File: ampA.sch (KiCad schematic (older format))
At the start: 13 parts, among them U2 screw_term, U3 screw_term, U4 screw_term, U7 TL084

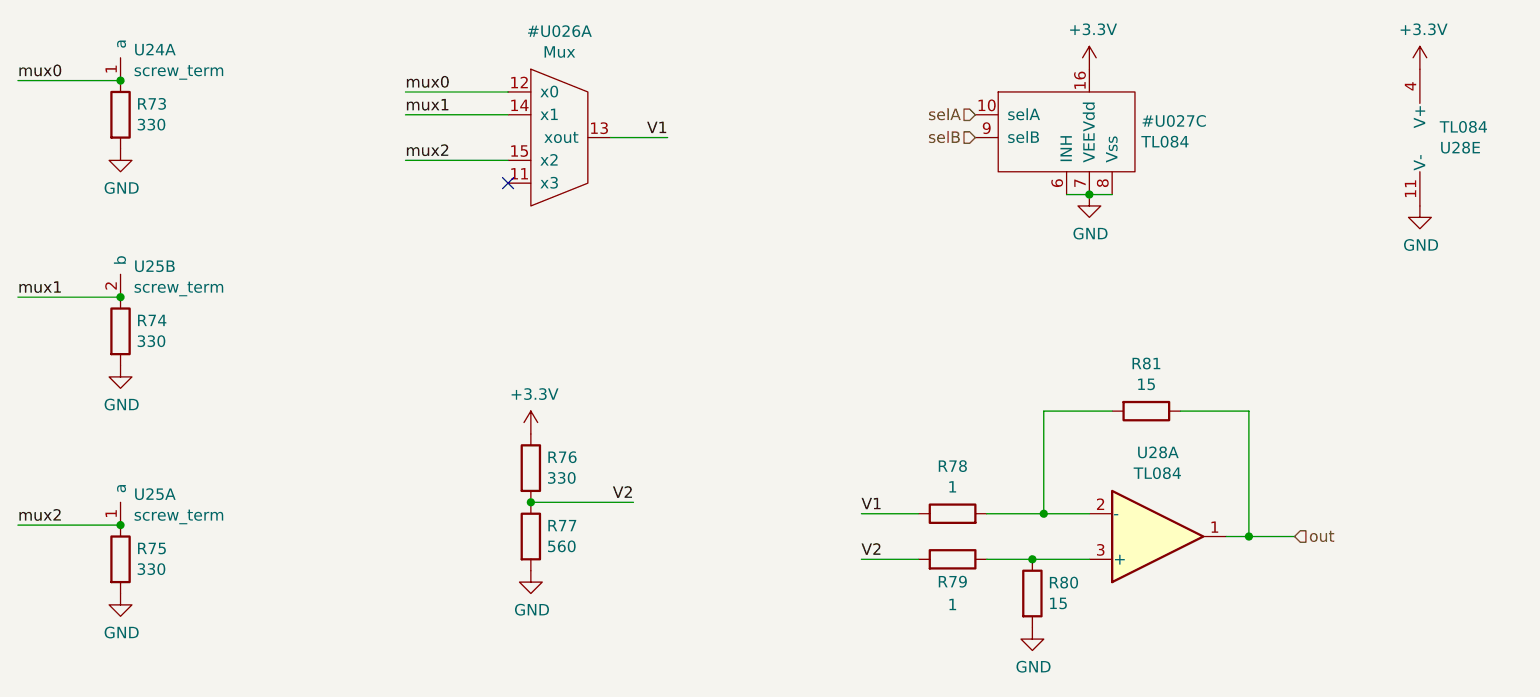
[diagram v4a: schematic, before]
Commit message: added footprint to some op amps
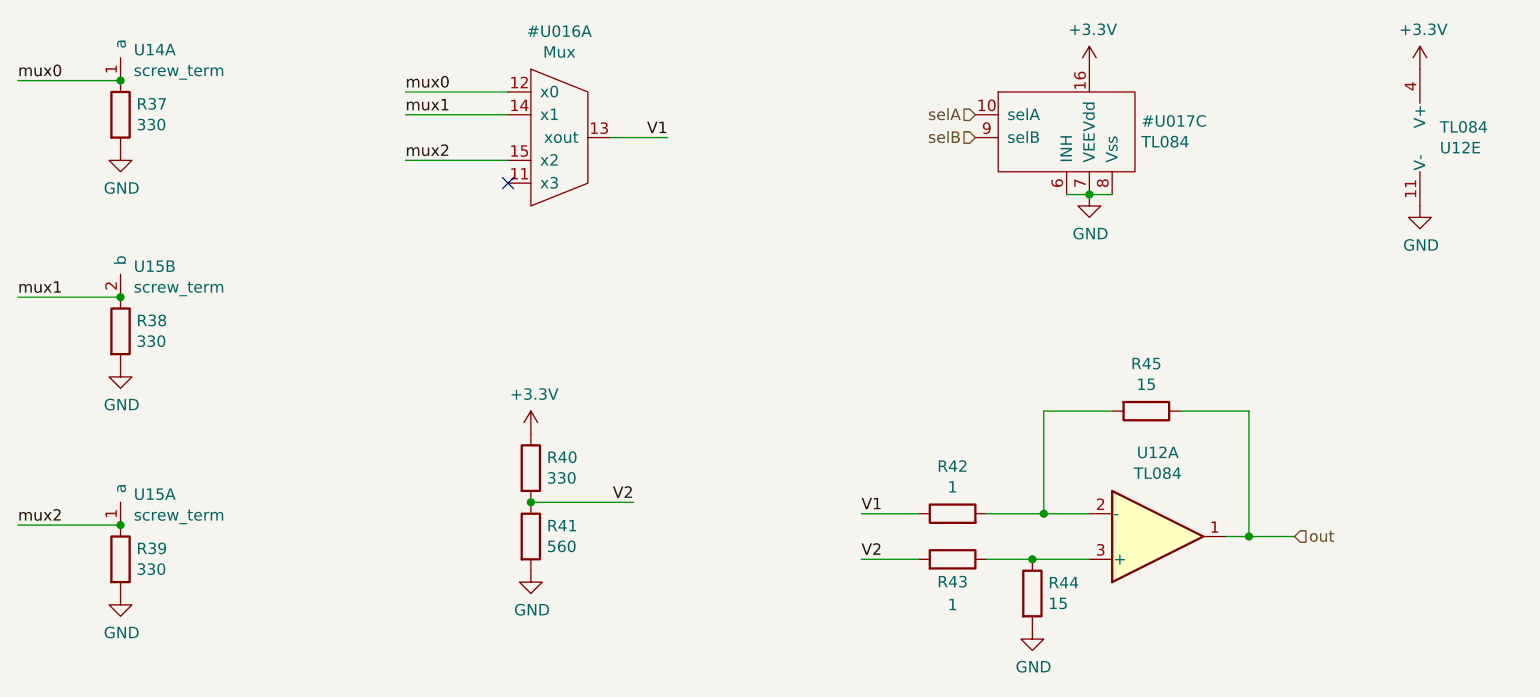
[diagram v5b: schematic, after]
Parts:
- U7: footprint (none) -> Package_DIP:DIP-14_W7.62mm
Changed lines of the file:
@@
 AR Path="/601B4C0E/6013BAC9" Ref="#PWR038"  Part="1"
 AR Path="/601B73B7/6013BAC9" Ref="#PWR068"  Part="1"
-F 0 "#PWR068" H 1450 1850 50  0001 C CNN
+F 0 "#PWR038" H 1450 1850 50  0001 C CNN
 F 1 "GND" H 1455 1927 50  0000 C CNN
 F 2 "" H 1450 2100 50  0001 C CNN
@@
 AR Path="/601B4C0E/60198F31" Ref="U12"  Part="1"
 AR Path="/601B73B7/60198F31" Ref="U28"  Part="1"
-F 0 "U28" H 6000 3433 50  0000 C CNN
+F 0 "U12" H 6000 3433 50  0000 C CNN
 F 1 "TL084" H 6000 3524 50  0000 C CNN
-F 2 "" H 5950 3900 50  0001 C CNN
+F 2 "Package_DIP:DIP-14_W7.62mm" H 5950 3900 50  0001 C CNN
 F 3 "http://www.ti.com/lit/ds/symlink/tl081.pdf" H 6050 4000 50  0001 C CNN
 	1    6000 3800
@@
 AR Path="/601B4C0E/6019D565" Ref="R44"  Part="1"
 AR Path="/601B73B7/6019D565" Ref="R80"  Part="1"
-F 0 "R80" H 5520 4096 50  0000 L CNN
+F 0 "R44" H 5520 4096 50  0000 L CNN
 F 1 "15" H 5520 4005 50  0000 L CNN
 F 2 "Resistor_THT:R_Axial_DIN0204_L3.6mm_D1.6mm_P5.08mm_Horizontal" V 5380 4050 50  0001 C CNN
@@
 AR Path="/601B4C0E/60198F32" Ref="R45"  Part="1"
 AR Path="/601B73B7/60198F32" Ref="R81"  Part="1"
-F 0 "R81" V 5743 3250 50  0000 C CNN
+F 0 "R45" V 5743 3250 50  0000 C CNN
 F 1 "15" V 5834 3250 50  0000 C CNN
 F 2 "Resistor_THT:R_Axial_DIN0204_L3.6mm_D1.6mm_P5.08mm_Horizontal" V 5880 3250 50  0001 C CNN
@@
 AR Path="/601B4C0E/6017E431" Ref="R42"  Part="1"
 AR Path="/601B73B7/6017E431" Ref="R78"  Part="1"
-F 0 "R78" V 5307 3700 50  0000 C CNN
+F 0 "R42" V 5307 3700 50  0000 C CNN
 F 1 "1" V 5216 3700 50  0000 C CNN
 F 2 "Resistor_THT:R_Axial_DIN0204_L3.6mm_D1.6mm_P5.08mm_Horizontal" V 5030 3700 50  0001 C CNN
@@
 AR Path="/601B4C0E/6019D568" Ref="R43"  Part="1"
 AR Path="/601B73B7/6019D568" Ref="R79"  Part="1"
-F 0 "R79" V 5000 3900 50  0000 C CNN
+F 0 "R43" V 5000 3900 50  0000 C CNN
 F 1 "1" V 4900 3900 50  0000 C CNN
 F 2 "Resistor_THT:R_Axial_DIN0204_L3.6mm_D1.6mm_P5.08mm_Horizontal" V 5030 3900 50  0001 C CNN
@@
 AR Path="/601B4C0E/6019D55E" Ref="R40"  Part="1"
 AR Path="/601B73B7/6019D55E" Ref="R76"  Part="1"
-F 0 "R76" H 3320 3546 50  0000 L CNN
+F 0 "R40" H 3320 3546 50  0000 L CNN
 F 1 "330" H 3320 3455 50  0000 L CNN
 F 2 "Resistor_THT:R_Axial_DIN0204_L3.6mm_D1.6mm_P5.08mm_Horizontal" V 3180 3500 50  0001 C CNN
@@
 AR Path="/601B4C0E/6019D55F" Ref="R41"  Part="1"
 AR Path="/601B73B7/6019D55F" Ref="R77"  Part="1"
-F 0 "R77" H 3320 3846 50  0000 L CNN
+F 0 "R41" H 3320 3846 50  0000 L CNN
 F 1 "560" H 3320 3755 50  0000 L CNN
 F 2 "Resistor_THT:R_Axial_DIN0204_L3.6mm_D1.6mm_P5.08mm_Horizontal" V 3180 3800 50  0001 C CNN
@@
 AR Path="/601B4C0E/6019D560" Ref="#PWR041"  Part="1"
 AR Path="/601B73B7/6019D560" Ref="#PWR071"  Part="1"
-F 0 "#PWR071" H 3250 3200 50  0001 C CNN
+F 0 "#PWR041" H 3250 3200 50  0001 C CNN
 F 1 "+3.3V" H 3265 3523 50  0000 C CNN
 F 2 "" H 3250 3350 50  0001 C CNN
@@
 AR Path="/601B4C0E/60198F38" Ref="#PWR042"  Part="1"
 AR Path="/601B73B7/60198F38" Ref="#PWR072"  Part="1"
-F 0 "#PWR072" H 3250 3700 50  0001 C CNN
+F 0 "#PWR042" H 3250 3700 50  0001 C CNN
 F 1 "GND" H 3255 3777 50  0000 C CNN
 F 2 "" H 3250 3950 50  0001 C CNN
@@
 AR Path="/601B4C0E/6016B854" Ref="#PWR043"  Part="1"
 AR Path="/601B73B7/6016B854" Ref="#PWR073"  Part="1"
-F 0 "#PWR073" H 5450 3950 50  0001 C CNN
+F 0 "#PWR043" H 5450 3950 50  0001 C CNN
 F 1 "GND" H 5455 4027 50  0000 C CNN
 F 2 "" H 5450 4200 50  0001 C CNN
@@
 AR Path="/601B4C0E/6016D691" Ref="R37"  Part="1"
 AR Path="/601B73B7/6016D691" Ref="R73"  Part="1"
-F 0 "R73" H 1520 1996 50  0000 L CNN
+F 0 "R37" H 1520 1996 50  0000 L CNN
 F 1 "330" H 1520 1905 50  0000 L CNN
 F 2 "Resistor_THT:R_Axial_DIN0204_L3.6mm_D1.6mm_P5.08mm_Horizontal" V 1380 1950 50  0001 C CNN
@@
 AR Path="/601B4C0E/601709E6" Ref="#U016"  Part="1"
 AR Path="/601B73B7/601709E6" Ref="#U026"  Part="1"
-F 0 "#U026" H 3375 2515 50  0000 C CNN
+F 0 "#U016" H 3375 2515 50  0000 C CNN
 F 1 "Mux" H 3375 2424 50  0000 C CNN
 F 2 "Package_DIP:DIP-14_W7.62mm" H 3350 2050 50  0001 C CNN
@@
 AR Path="/601B4C0E/6016FA62" Ref="U14"  Part="1"
 AR Path="/601B73B7/6016FA62" Ref="U24"  Part="1"
-F 0 "U24" H 1508 1934 50  0000 L CNN
+F 0 "U14" H 1508 1934 50  0000 L CNN
 F 1 "screw_term" H 1508 1843 50  0000 L CNN
 F 2 "Connector_PinHeader_1.27mm:PinHeader_1x02_P1.27mm_Vertical" H 1450 1800 50  0001 C CNN
@@
 AR Path="/601B4C0E/6019D559" Ref="#PWR039"  Part="1"
 AR Path="/601B73B7/6019D559" Ref="#PWR069"  Part="1"
-F 0 "#PWR069" H 1450 2800 50  0001 C CNN
+F 0 "#PWR039" H 1450 2800 50  0001 C CNN
 F 1 "GND" H 1455 2877 50  0000 C CNN
 F 2 "" H 1450 3050 50  0001 C CNN
@@
 AR Path="/601B4C0E/6019D56A" Ref="R38"  Part="1"
 AR Path="/601B73B7/6019D56A" Ref="R74"  Part="1"
-F 0 "R74" H 1520 2946 50  0000 L CNN
+F 0 "R38" H 1520 2946 50  0000 L CNN
 F 1 "330" H 1520 2855 50  0000 L CNN
 F 2 "Resistor_THT:R_Axial_DIN0204_L3.6mm_D1.6mm_P5.08mm_Horizontal" V 1380 2900 50  0001 C CNN
@@
 AR Path="/601B4C0E/60176F25" Ref="U15"  Part="2"
 AR Path="/601B73B7/60176F25" Ref="U25"  Part="2"
-F 0 "U25" H 1508 2884 50  0000 L CNN
+F 0 "U15" H 1508 2884 50  0000 L CNN
 F 1 "screw_term" H 1508 2793 50  0000 L CNN
 F 2 "Connector_PinHeader_1.27mm:PinHeader_1x02_P1.27mm_Vertical" H 1450 2750 50  0001 C CNN
@@
 AR Path="/601B4C0E/6019D55B" Ref="#PWR040"  Part="1"
 AR Path="/601B73B7/6019D55B" Ref="#PWR070"  Part="1"
-F 0 "#PWR070" H 1450 3800 50  0001 C CNN
+F 0 "#PWR040" H 1450 3800 50  0001 C CNN
 F 1 "GND" H 1455 3877 50  0000 C CNN
 F 2 "" H 1450 4050 50  0001 C CNN
@@
 AR Path="/601B4C0E/6017E43F" Ref="R39"  Part="1"
 AR Path="/601B73B7/6017E43F" Ref="R75"  Part="1"
-F 0 "R75" H 1520 3946 50  0000 L CNN
+F 0 "R39" H 1520 3946 50  0000 L CNN
 F 1 "330" H 1520 3855 50  0000 L CNN
 F 2 "Resistor_THT:R_Axial_DIN0204_L3.6mm_D1.6mm_P5.08mm_Horizontal" V 1380 3900 50  0001 C CNN
@@
 AR Path="/601B4C0E/6019D55C" Ref="U15"  Part="1"
 AR Path="/601B73B7/6019D55C" Ref="U25"  Part="1"
-F 0 "U25" H 1508 3884 50  0000 L CNN
+F 0 "U15" H 1508 3884 50  0000 L CNN
 F 1 "screw_term" H 1508 3793 50  0000 L CNN
 F 2 "Connector_PinHeader_1.27mm:PinHeader_1x02_P1.27mm_Vertical" H 1450 3750 50  0001 C CNN
@@
 AR Path="/601B4C0E/60186A46" Ref="#U017"  Part="3"
 AR Path="/601B73B7/60186A46" Ref="#U027"  Part="3"
-F 0 "#U027" H 5928 2221 50  0000 L CNN
+F 0 "#U017" H 5928 2221 50  0000 L CNN
 F 1 "TL084" H 5928 2130 50  0000 L CNN
 F 2 "" H 5700 2100 50  0001 C CNN
@@
 AR Path="/601B4C0E/601899DD" Ref="#PWR045"  Part="1"
 AR Path="/601B73B7/601899DD" Ref="#PWR075"  Part="1"
-F 0 "#PWR075" H 5700 2050 50  0001 C CNN
+F 0 "#PWR045" H 5700 2050 50  0001 C CNN
 F 1 "GND" H 5705 2127 50  0000 C CNN
 F 2 "" H 5700 2300 50  0001 C CNN
@@
 AR Path="/601B4C0E/60189E9E" Ref="#PWR044"  Part="1"
 AR Path="/601B73B7/60189E9E" Ref="#PWR074"  Part="1"
-F 0 "#PWR074" H 5700 1600 50  0001 C CNN
+F 0 "#PWR044" H 5700 1600 50  0001 C CNN
 F 1 "+3.3V" H 5715 1923 50  0000 C CNN
 F 2 "" H 5700 1750 50  0001 C CNN
@@
 AR Path="/601B4C0E/60194917" Ref="U12"  Part="5"
 AR Path="/601B73B7/60194917" Ref="U28"  Part="5"
-F 0 "U28" H 6863 2004 50  0000 R CNN
+F 0 "U12" H 6863 2004 50  0000 R CNN
 F 1 "TL084" H 6863 2095 50  0000 R CNN
-F 2 "" H 7000 2150 50  0001 C CNN
+F 2 "Package_DIP:DIP-14_W7.62mm" H 7000 2150 50  0001 C CNN
 F 3 "http://www.ti.com/lit/ds/symlink/tl081.pdf" H 7100 2250 50  0001 C CNN
 	5    7050 2050
@@
 AR Path="/601B4C0E/60195FF1" Ref="#PWR047"  Part="1"
 AR Path="/601B73B7/60195FF1" Ref="#PWR077"  Part="1"
-F 0 "#PWR077" H 7150 2100 50  0001 C CNN
+F 0 "#PWR047" H 7150 2100 50  0001 C CNN
 F 1 "GND" H 7155 2177 50  0000 C CNN
 F 2 "" H 7150 2350 50  0001 C CNN
@@
 AR Path="/601B4C0E/60198969" Ref="#PWR046"  Part="1"
 AR Path="/601B73B7/60198969" Ref="#PWR076"  Part="1"
-F 0 "#PWR076" H 7150 1600 50  0001 C CNN
+F 0 "#PWR046" H 7150 1600 50  0001 C CNN
 F 1 "+3.3V" H 7165 1923 50  0000 C CNN
 F 2 "" H 7150 1750 50  0001 C CNN

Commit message: updated all mux packages in eeschema
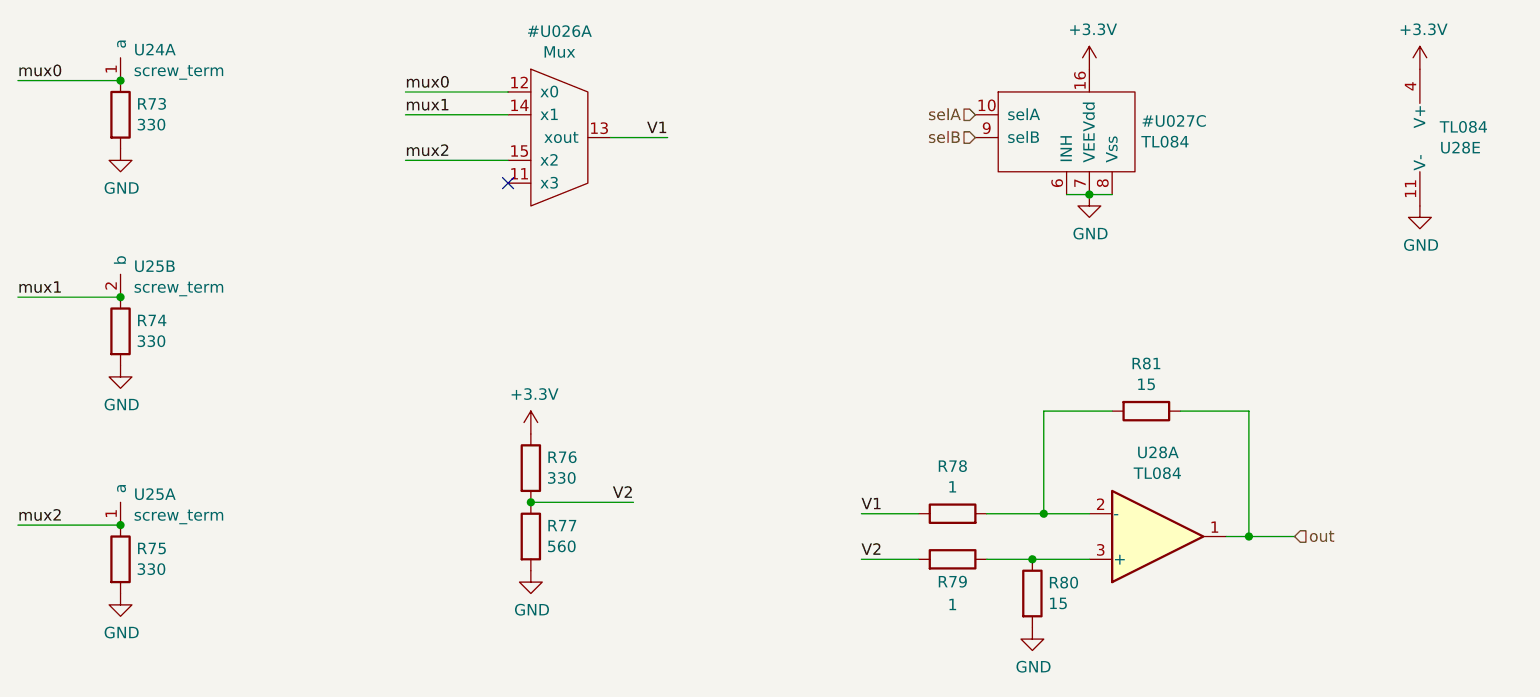
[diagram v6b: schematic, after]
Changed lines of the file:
@@
 $Descr A4 11693 8268
 encoding utf-8
-Sheet 6 11
+Sheet 10 11
 Title ""
 Date ""
@@
 AR Path="/601B4C0E/6013BAC9" Ref="#PWR038"  Part="1"
 AR Path="/601B73B7/6013BAC9" Ref="#PWR068"  Part="1"
-F 0 "#PWR038" H 1450 1850 50  0001 C CNN
+F 0 "#PWR068" H 1450 1850 50  0001 C CNN
 F 1 "GND" H 1455 1927 50  0000 C CNN
 F 2 "" H 1450 2100 50  0001 C CNN
@@
 AR Path="/601B4C0E/60198F31" Ref="U12"  Part="1"
 AR Path="/601B73B7/60198F31" Ref="U28"  Part="1"
-F 0 "U12" H 6000 3433 50  0000 C CNN
+F 0 "U28" H 6000 3433 50  0000 C CNN
 F 1 "TL084" H 6000 3524 50  0000 C CNN
 F 2 "Package_DIP:DIP-14_W7.62mm" H 5950 3900 50  0001 C CNN
@@
 AR Path="/601B4C0E/6019D565" Ref="R44"  Part="1"
 AR Path="/601B73B7/6019D565" Ref="R80"  Part="1"
-F 0 "R44" H 5520 4096 50  0000 L CNN
+F 0 "R80" H 5520 4096 50  0000 L CNN
 F 1 "15" H 5520 4005 50  0000 L CNN
 F 2 "Resistor_THT:R_Axial_DIN0204_L3.6mm_D1.6mm_P5.08mm_Horizontal" V 5380 4050 50  0001 C CNN
@@
 AR Path="/601B4C0E/60198F32" Ref="R45"  Part="1"
 AR Path="/601B73B7/60198F32" Ref="R81"  Part="1"
-F 0 "R45" V 5743 3250 50  0000 C CNN
+F 0 "R81" V 5743 3250 50  0000 C CNN
 F 1 "15" V 5834 3250 50  0000 C CNN
 F 2 "Resistor_THT:R_Axial_DIN0204_L3.6mm_D1.6mm_P5.08mm_Horizontal" V 5880 3250 50  0001 C CNN
@@
 AR Path="/601B4C0E/6017E431" Ref="R42"  Part="1"
 AR Path="/601B73B7/6017E431" Ref="R78"  Part="1"
-F 0 "R42" V 5307 3700 50  0000 C CNN
+F 0 "R78" V 5307 3700 50  0000 C CNN
 F 1 "1" V 5216 3700 50  0000 C CNN
 F 2 "Resistor_THT:R_Axial_DIN0204_L3.6mm_D1.6mm_P5.08mm_Horizontal" V 5030 3700 50  0001 C CNN
@@
 AR Path="/601B4C0E/6019D568" Ref="R43"  Part="1"
 AR Path="/601B73B7/6019D568" Ref="R79"  Part="1"
-F 0 "R43" V 5000 3900 50  0000 C CNN
+F 0 "R79" V 5000 3900 50  0000 C CNN
 F 1 "1" V 4900 3900 50  0000 C CNN
 F 2 "Resistor_THT:R_Axial_DIN0204_L3.6mm_D1.6mm_P5.08mm_Horizontal" V 5030 3900 50  0001 C CNN
@@
 AR Path="/601B4C0E/6019D55E" Ref="R40"  Part="1"
 AR Path="/601B73B7/6019D55E" Ref="R76"  Part="1"
-F 0 "R40" H 3320 3546 50  0000 L CNN
+F 0 "R76" H 3320 3546 50  0000 L CNN
 F 1 "330" H 3320 3455 50  0000 L CNN
 F 2 "Resistor_THT:R_Axial_DIN0204_L3.6mm_D1.6mm_P5.08mm_Horizontal" V 3180 3500 50  0001 C CNN
@@
 AR Path="/601B4C0E/6019D55F" Ref="R41"  Part="1"
 AR Path="/601B73B7/6019D55F" Ref="R77"  Part="1"
-F 0 "R41" H 3320 3846 50  0000 L CNN
+F 0 "R77" H 3320 3846 50  0000 L CNN
 F 1 "560" H 3320 3755 50  0000 L CNN
 F 2 "Resistor_THT:R_Axial_DIN0204_L3.6mm_D1.6mm_P5.08mm_Horizontal" V 3180 3800 50  0001 C CNN
@@
 AR Path="/601B4C0E/6019D560" Ref="#PWR041"  Part="1"
 AR Path="/601B73B7/6019D560" Ref="#PWR071"  Part="1"
-F 0 "#PWR041" H 3250 3200 50  0001 C CNN
+F 0 "#PWR071" H 3250 3200 50  0001 C CNN
 F 1 "+3.3V" H 3265 3523 50  0000 C CNN
 F 2 "" H 3250 3350 50  0001 C CNN
@@
 AR Path="/601B4C0E/60198F38" Ref="#PWR042"  Part="1"
 AR Path="/601B73B7/60198F38" Ref="#PWR072"  Part="1"
-F 0 "#PWR042" H 3250 3700 50  0001 C CNN
+F 0 "#PWR072" H 3250 3700 50  0001 C CNN
 F 1 "GND" H 3255 3777 50  0000 C CNN
 F 2 "" H 3250 3950 50  0001 C CNN
@@
 AR Path="/601B4C0E/6016B854" Ref="#PWR043"  Part="1"
 AR Path="/601B73B7/6016B854" Ref="#PWR073"  Part="1"
-F 0 "#PWR043" H 5450 3950 50  0001 C CNN
+F 0 "#PWR073" H 5450 3950 50  0001 C CNN
 F 1 "GND" H 5455 4027 50  0000 C CNN
 F 2 "" H 5450 4200 50  0001 C CNN
@@
 AR Path="/601B4C0E/6016D691" Ref="R37"  Part="1"
 AR Path="/601B73B7/6016D691" Ref="R73"  Part="1"
-F 0 "R37" H 1520 1996 50  0000 L CNN
+F 0 "R73" H 1520 1996 50  0000 L CNN
 F 1 "330" H 1520 1905 50  0000 L CNN
 F 2 "Resistor_THT:R_Axial_DIN0204_L3.6mm_D1.6mm_P5.08mm_Horizontal" V 1380 1950 50  0001 C CNN
@@
 AR Path="/601B4C0E/601709E6" Ref="#U016"  Part="1"
 AR Path="/601B73B7/601709E6" Ref="#U026"  Part="1"
-F 0 "#U016" H 3375 2515 50  0000 C CNN
+F 0 "#U026" H 3375 2515 50  0000 C CNN
 F 1 "Mux" H 3375 2424 50  0000 C CNN
-F 2 "Package_DIP:DIP-14_W7.62mm" H 3350 2050 50  0001 C CNN
+F 2 "Package_DIP:DIP-16_W7.62mm" H 3350 2050 50  0001 C CNN
 F 3 "" H 3350 2050 50  0001 C CNN
 	1    3350 2050
@@
 AR Path="/601B4C0E/6016FA62" Ref="U14"  Part="1"
 AR Path="/601B73B7/6016FA62" Ref="U24"  Part="1"
-F 0 "U14" H 1508 1934 50  0000 L CNN
+F 0 "U24" H 1508 1934 50  0000 L CNN
 F 1 "screw_term" H 1508 1843 50  0000 L CNN
 F 2 "Connector_PinHeader_1.27mm:PinHeader_1x02_P1.27mm_Vertical" H 1450 1800 50  0001 C CNN
@@
 AR Path="/601B4C0E/6019D559" Ref="#PWR039"  Part="1"
 AR Path="/601B73B7/6019D559" Ref="#PWR069"  Part="1"
-F 0 "#PWR039" H 1450 2800 50  0001 C CNN
+F 0 "#PWR069" H 1450 2800 50  0001 C CNN
 F 1 "GND" H 1455 2877 50  0000 C CNN
 F 2 "" H 1450 3050 50  0001 C CNN
@@
 AR Path="/601B4C0E/6019D56A" Ref="R38"  Part="1"
 AR Path="/601B73B7/6019D56A" Ref="R74"  Part="1"
-F 0 "R38" H 1520 2946 50  0000 L CNN
+F 0 "R74" H 1520 2946 50  0000 L CNN
 F 1 "330" H 1520 2855 50  0000 L CNN
 F 2 "Resistor_THT:R_Axial_DIN0204_L3.6mm_D1.6mm_P5.08mm_Horizontal" V 1380 2900 50  0001 C CNN
@@
 AR Path="/601B4C0E/60176F25" Ref="U15"  Part="2"
 AR Path="/601B73B7/60176F25" Ref="U25"  Part="2"
-F 0 "U15" H 1508 2884 50  0000 L CNN
+F 0 "U25" H 1508 2884 50  0000 L CNN
 F 1 "screw_term" H 1508 2793 50  0000 L CNN
 F 2 "Connector_PinHeader_1.27mm:PinHeader_1x02_P1.27mm_Vertical" H 1450 2750 50  0001 C CNN
@@
 AR Path="/601B4C0E/6019D55B" Ref="#PWR040"  Part="1"
 AR Path="/601B73B7/6019D55B" Ref="#PWR070"  Part="1"
-F 0 "#PWR040" H 1450 3800 50  0001 C CNN
+F 0 "#PWR070" H 1450 3800 50  0001 C CNN
 F 1 "GND" H 1455 3877 50  0000 C CNN
 F 2 "" H 1450 4050 50  0001 C CNN
@@
 AR Path="/601B4C0E/6017E43F" Ref="R39"  Part="1"
 AR Path="/601B73B7/6017E43F" Ref="R75"  Part="1"
-F 0 "R39" H 1520 3946 50  0000 L CNN
+F 0 "R75" H 1520 3946 50  0000 L CNN
 F 1 "330" H 1520 3855 50  0000 L CNN
 F 2 "Resistor_THT:R_Axial_DIN0204_L3.6mm_D1.6mm_P5.08mm_Horizontal" V 1380 3900 50  0001 C CNN
@@
 AR Path="/601B4C0E/6019D55C" Ref="U15"  Part="1"
 AR Path="/601B73B7/6019D55C" Ref="U25"  Part="1"
-F 0 "U15" H 1508 3884 50  0000 L CNN
+F 0 "U25" H 1508 3884 50  0000 L CNN
 F 1 "screw_term" H 1508 3793 50  0000 L CNN
 F 2 "Connector_PinHeader_1.27mm:PinHeader_1x02_P1.27mm_Vertical" H 1450 3750 50  0001 C CNN
@@
 AR Path="/601B4C0E/60186A46" Ref="#U017"  Part="3"
 AR Path="/601B73B7/60186A46" Ref="#U027"  Part="3"
-F 0 "#U017" H 5928 2221 50  0000 L CNN
+F 0 "#U027" H 5928 2221 50  0000 L CNN
 F 1 "TL084" H 5928 2130 50  0000 L CNN
 F 2 "" H 5700 2100 50  0001 C CNN
@@
 AR Path="/601B4C0E/601899DD" Ref="#PWR045"  Part="1"
 AR Path="/601B73B7/601899DD" Ref="#PWR075"  Part="1"
-F 0 "#PWR045" H 5700 2050 50  0001 C CNN
+F 0 "#PWR075" H 5700 2050 50  0001 C CNN
 F 1 "GND" H 5705 2127 50  0000 C CNN
 F 2 "" H 5700 2300 50  0001 C CNN
@@
 AR Path="/601B4C0E/60189E9E" Ref="#PWR044"  Part="1"
 AR Path="/601B73B7/60189E9E" Ref="#PWR074"  Part="1"
-F 0 "#PWR044" H 5700 1600 50  0001 C CNN
+F 0 "#PWR074" H 5700 1600 50  0001 C CNN
 F 1 "+3.3V" H 5715 1923 50  0000 C CNN
 F 2 "" H 5700 1750 50  0001 C CNN
@@
 AR Path="/601B4C0E/60194917" Ref="U12"  Part="5"
 AR Path="/601B73B7/60194917" Ref="U28"  Part="5"
-F 0 "U12" H 6863 2004 50  0000 R CNN
+F 0 "U28" H 6863 2004 50  0000 R CNN
 F 1 "TL084" H 6863 2095 50  0000 R CNN
 F 2 "Package_DIP:DIP-14_W7.62mm" H 7000 2150 50  0001 C CNN
@@
 AR Path="/601B4C0E/60195FF1" Ref="#PWR047"  Part="1"
 AR Path="/601B73B7/60195FF1" Ref="#PWR077"  Part="1"
-F 0 "#PWR047" H 7150 2100 50  0001 C CNN
+F 0 "#PWR077" H 7150 2100 50  0001 C CNN
 F 1 "GND" H 7155 2177 50  0000 C CNN
 F 2 "" H 7150 2350 50  0001 C CNN
@@
 AR Path="/601B4C0E/60198969" Ref="#PWR046"  Part="1"
 AR Path="/601B73B7/60198969" Ref="#PWR076"  Part="1"
-F 0 "#PWR046" H 7150 1600 50  0001 C CNN
+F 0 "#PWR076" H 7150 1600 50  0001 C CNN
 F 1 "+3.3V" H 7165 1923 50  0000 C CNN
 F 2 "" H 7150 1750 50  0001 C CNN
